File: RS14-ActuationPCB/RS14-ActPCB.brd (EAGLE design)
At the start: 71.8 x 71.8 mm, 36 parts, among them IC1 L293D, IC2 L293D, P12V 22-23-2021, T1 2N3904, T2 2N3904, T3 2N3904, T4 2N3904

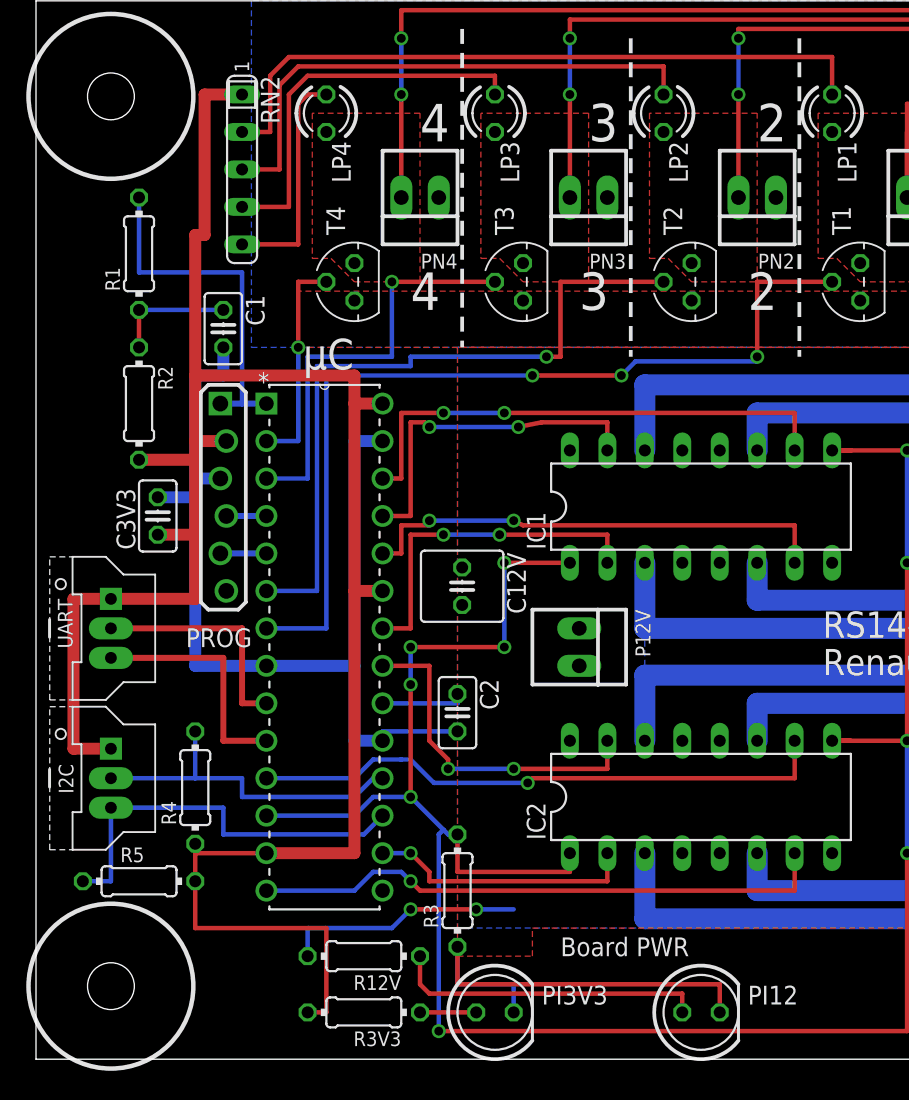
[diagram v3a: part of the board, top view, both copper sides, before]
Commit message: Battery Lockout PCB Added
This commit adds the current version of the Battery Lockout/Power Controller PCB to our design. It also includes revisions to the main actuation PCB to change the LEDs to the 3mm convention we addopted.
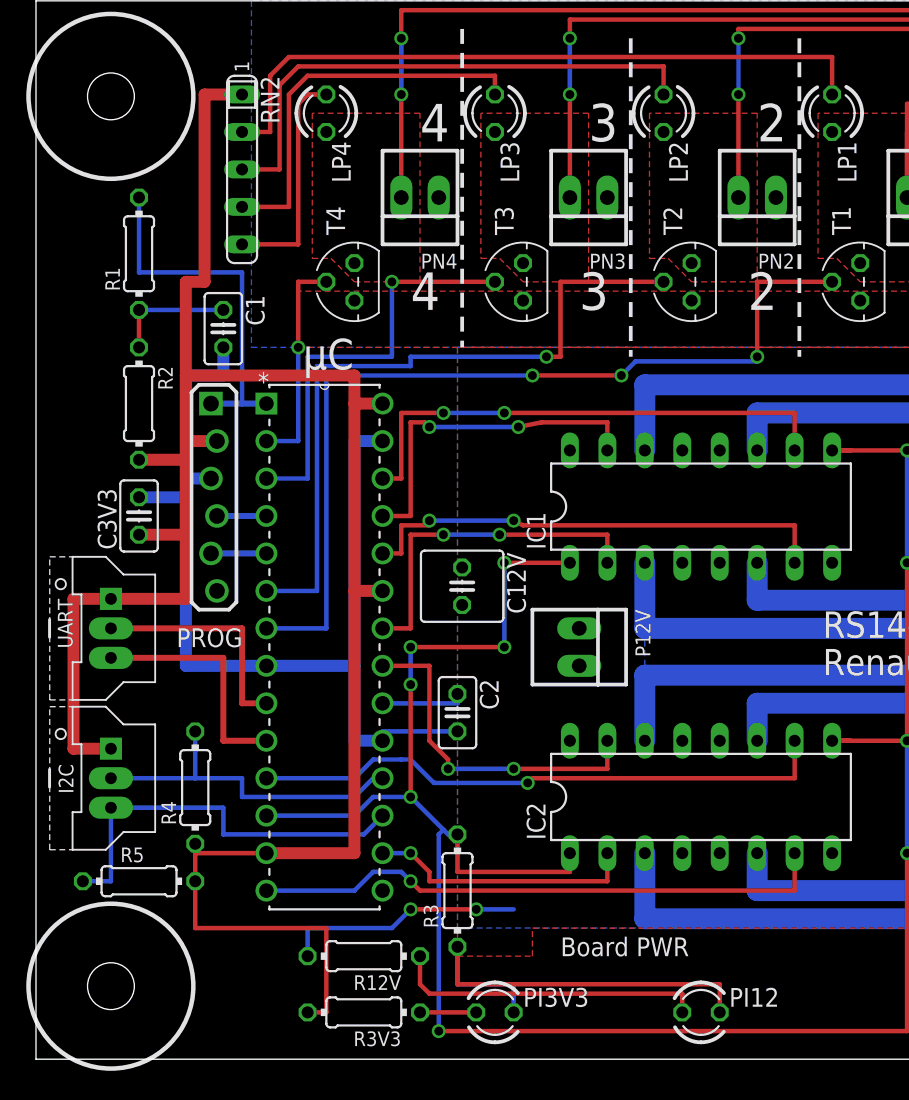
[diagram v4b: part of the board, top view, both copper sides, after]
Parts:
- PI12, PI3V3: device led:LED5MM -> led:LED3MM
- µC: value PIC32MX250F128B-I/SP -> PIC32MX250F128B
- moved C3V3 1.27 mm to (14.0, 49.5)
- moved PROG 0.63 mm to (19.1, 50.8)
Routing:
- net GND: track 98.9 -> 100.8 mm
- net 3V3: track 146.2 -> 146.8 mm
- net PGD: track 2.72 -> 3.35 mm
- net PGC: track 3.12 -> 3.76 mm
- net MCLR: track 24.1 -> 24.7 mm

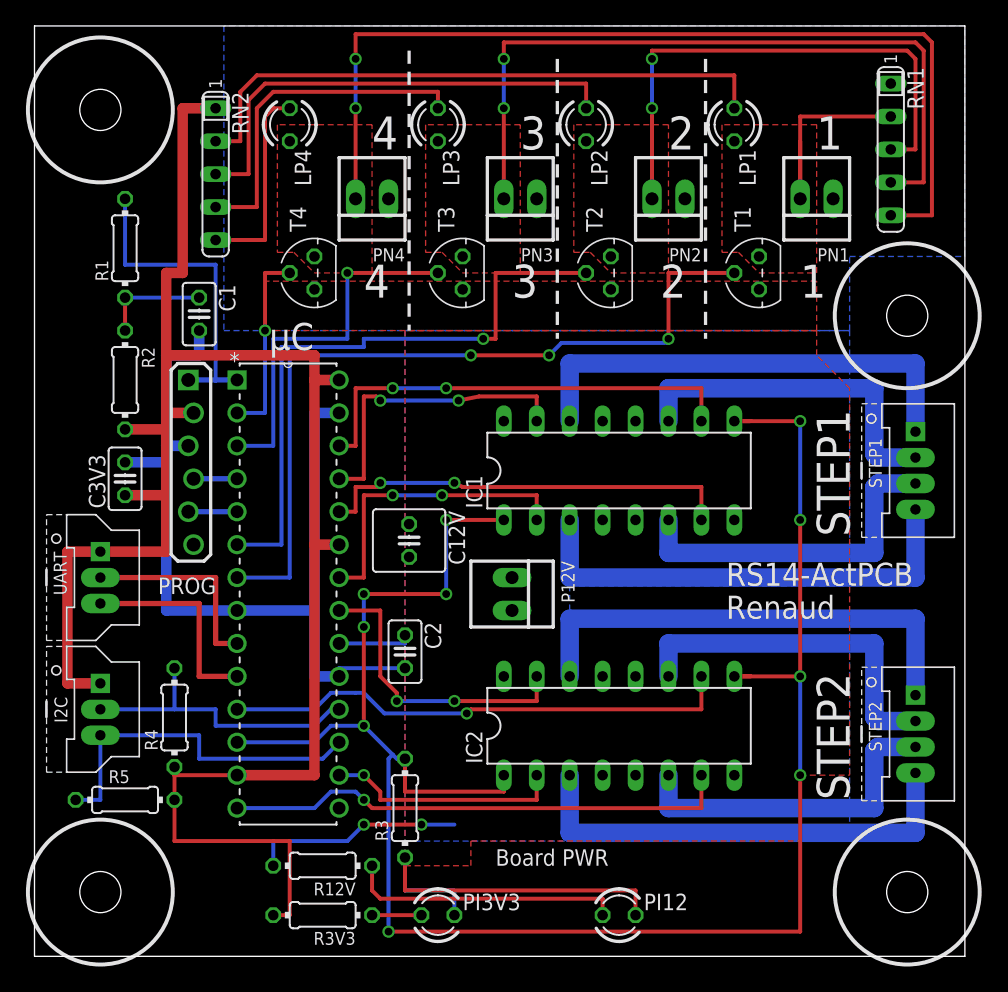
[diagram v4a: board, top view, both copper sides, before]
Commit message: Updated layouts for new hole sizes
Updated both boards to include proper sized holes for the screws (correction from 0.22" radius to 0.22" diamater clearance). This also includes some minor tweeks to clean up the board size a bit.
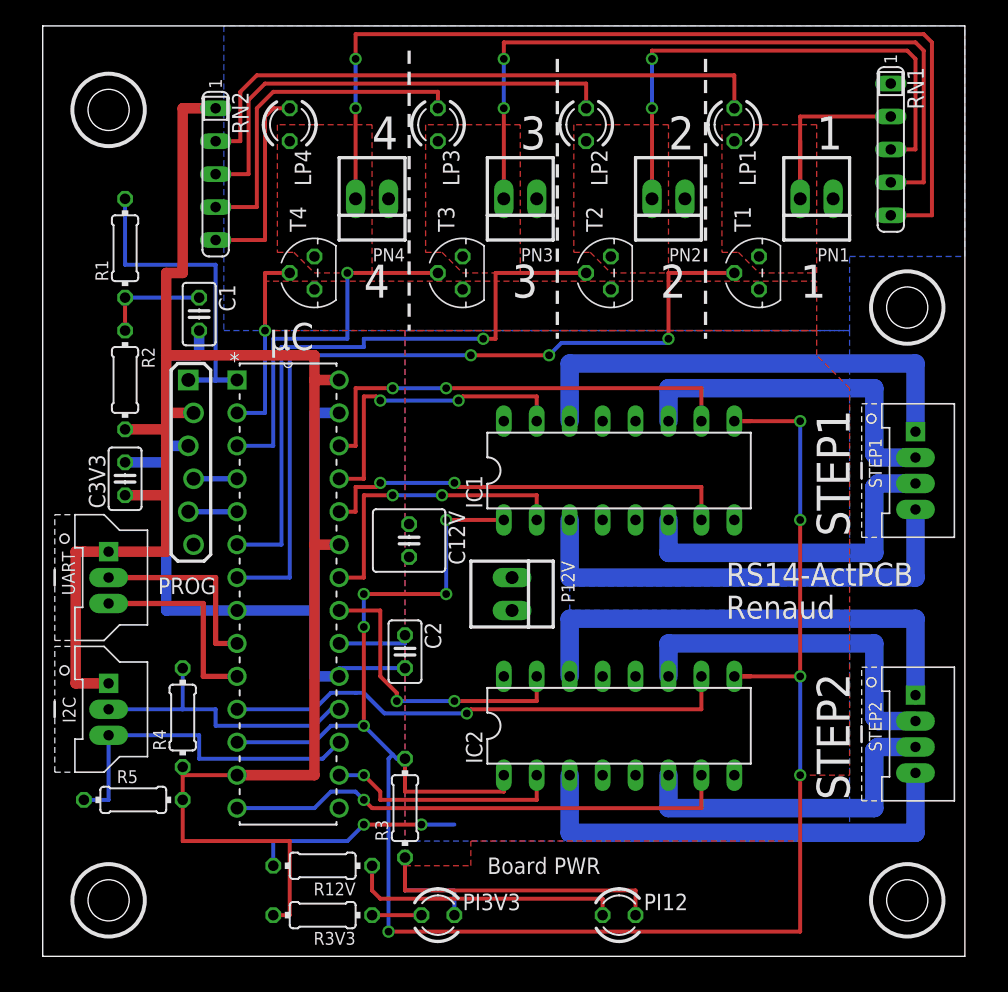
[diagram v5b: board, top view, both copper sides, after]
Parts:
- moved I2C 0.63 mm to (12.7, 31.8)
- moved R5 0.63 mm to (14.6, 24.8)
- moved UART 0.63 mm to (12.7, 41.9)
- moved R4 0.63 mm to (18.4, 31.1)
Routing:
- net 3V3: track 146.8 -> 144.9 mm
- net U1TX: track 16.2 -> 15.5 mm
- net U1RX: track 15.6 -> 15.0 mm
- net SDA: track 23.4 -> 22.8 mm
- net SCL: track 27.6 -> 27.0 mm
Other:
- board size 71.8 x 71.8 mm -> 71.1 x 71.8 mm
